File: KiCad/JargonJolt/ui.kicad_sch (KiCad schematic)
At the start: 0 parts

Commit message: worked on pinout
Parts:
- added C1, C2, C3: 0.1uF, symbol Device:C
- added R1, R3, R5: 1k, symbol Device:R
- added R2, R4, R6: 10k, symbol Device:R
- added SW1, SW2, SW3: SW_Push, symbol Switch:SW_Push
- added U1, U2, U3: 40106, symbol 4xxx:40106
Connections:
- new net: R3.2, R4.2, SW2.2
- new net: C1.1, R1.1, U1.1
- new net: R5.2, R6.2, SW3.2
- new net: C3.1, R5.1, U3.1
- new net: R1.2, R2.2, SW1.2
- new net: C2.1, R3.1, U2.1
- new net +3.3V: R2.1, R4.1, R6.1
- new net BUTTON1: U1.2
- new net BUTTON2: U2.2
- new net BUTTON3: U3.2
- new net GND: C1.2, C2.2, C3.2, SW1.1, SW2.1, SW3.1

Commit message: worked on schematic
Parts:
- added J4, J5: Conn_01x08, symbol Connector_Generic:Conn_01x08
- R2, R4, R6: value 10k -> 1M
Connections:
- net GND: now also R2.2, R4.2, R6.2, J4.2 (Pin_2), J5.2 (Pin_2); no longer SW1.1, SW2.1, SW3.1
- removed net +3.3V: R2.1, R4.1, R6.1
- new net: R3.2, R4.1, SW2.1
- new net: R5.2, R6.1, SW3.1
- new net: R1.2, R2.1, SW1.1
- new net +3.3VA: J4.1 (Pin_1), J5.1 (Pin_1), SW2.2, SW3.2
- new net BUSY1: J4.8 (Pin_8)
- new net BUSY2: J5.8 (Pin_8)
- new net CS1: J4.5 (Pin_5)
- new net CS2: J5.5 (Pin_5)
- new net DC1: J4.6 (Pin_6)
- new net DC2: J5.6 (Pin_6)
- new net MOSI: J4.3 (Pin_3), J5.3 (Pin_3)
- new net RST: J4.7 (Pin_7), J5.7 (Pin_7)
- new net SCLK: J4.4 (Pin_4), J5.4 (Pin_4)
- now unconnected: SW1.2
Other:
- note added: "Screen 1 Conn"
- note added: "Screen 2 Conn"
- moved on the sheet: R2, R4, R6, SW1, SW2, SW3

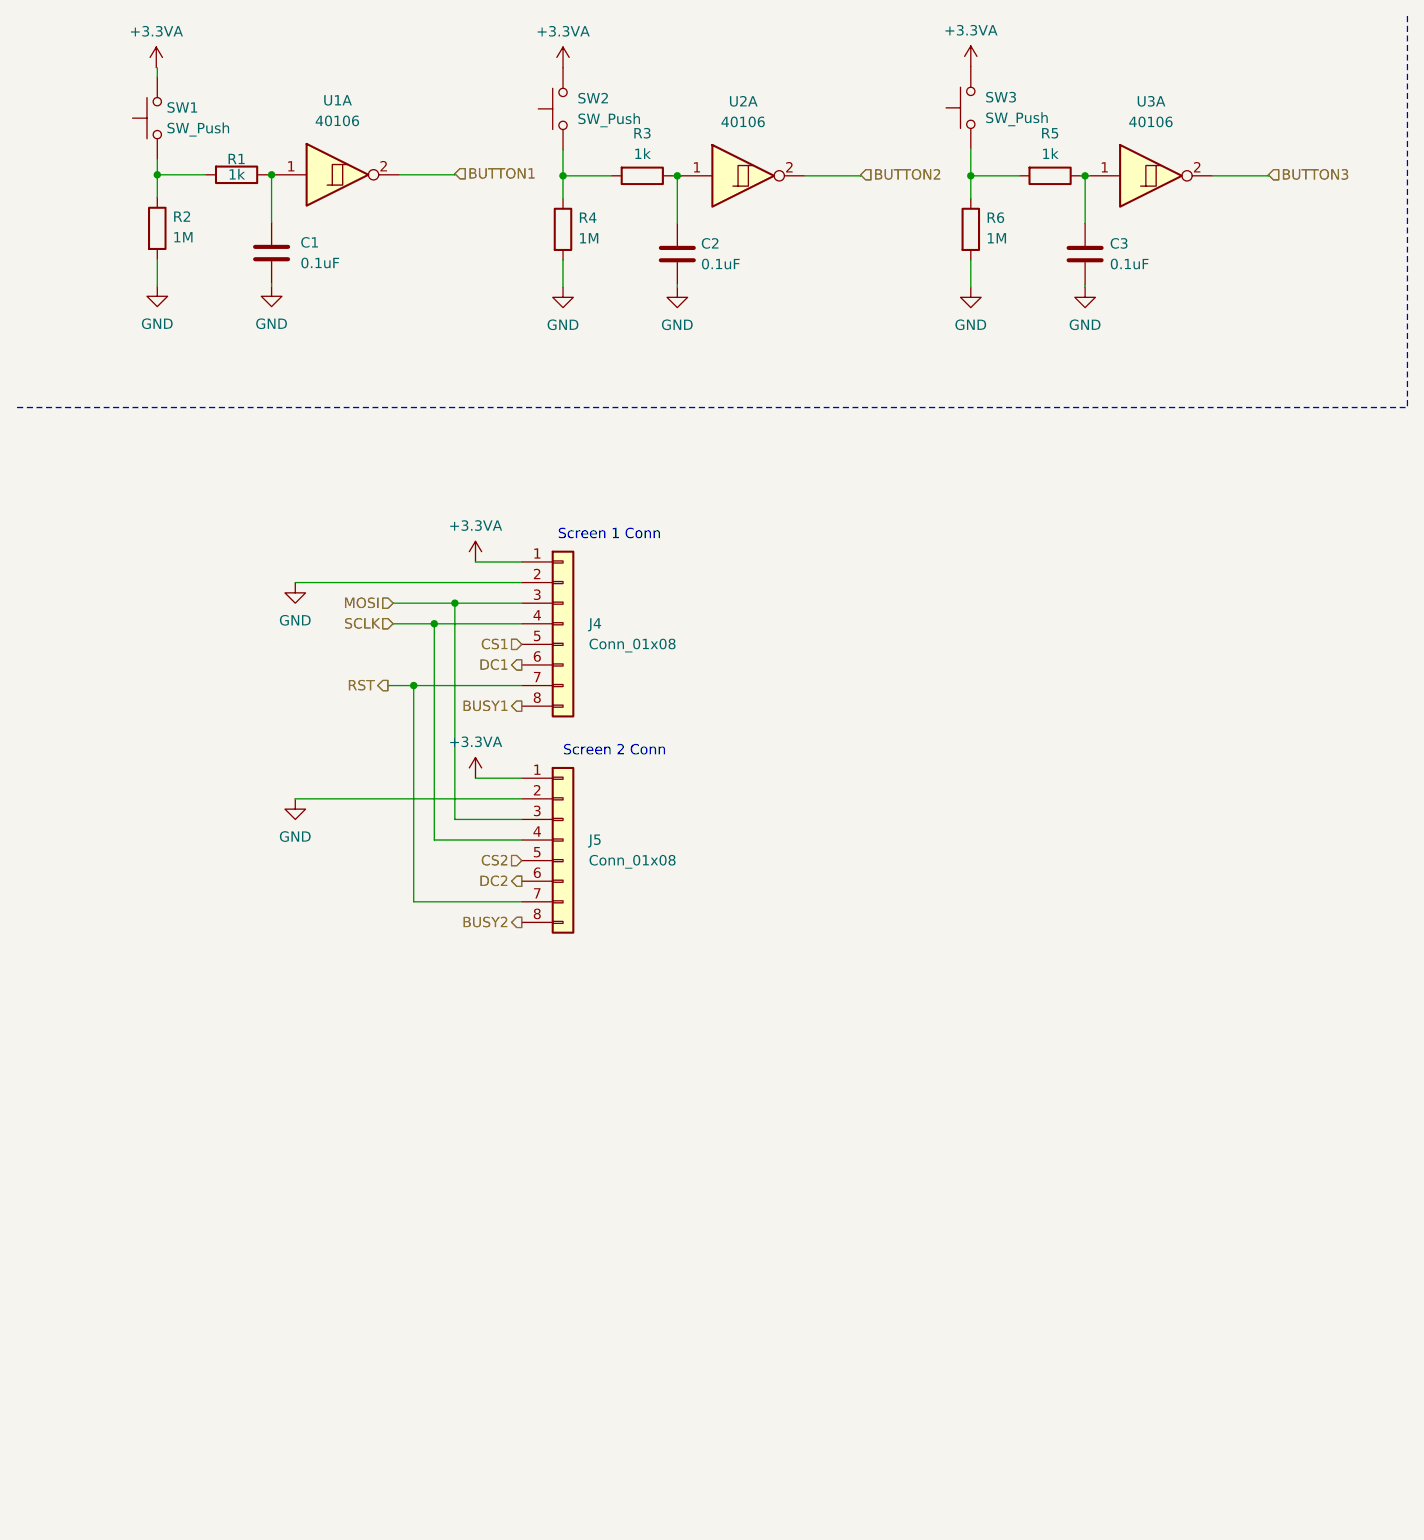
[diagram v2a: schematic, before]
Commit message: added i2s schematic
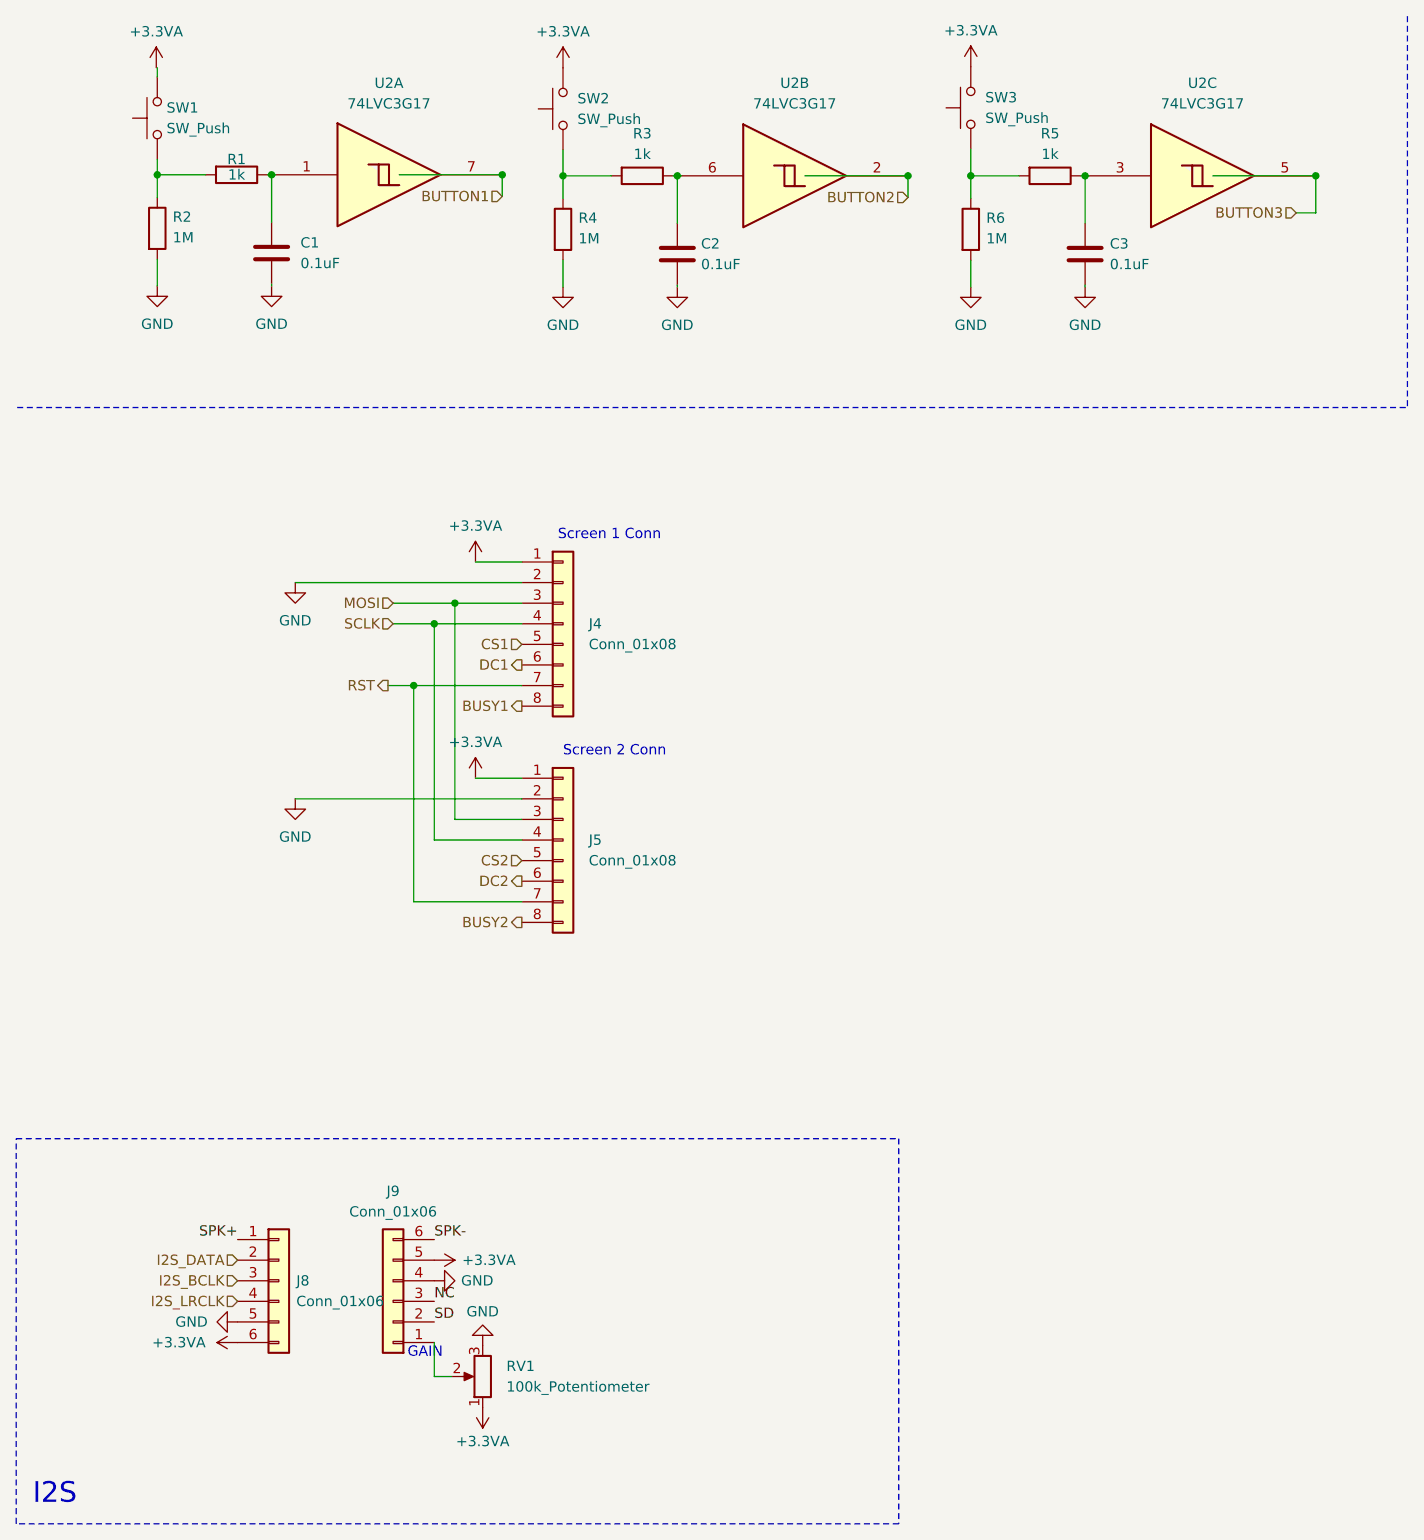
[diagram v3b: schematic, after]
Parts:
- removed U1, U2, U3: 40106, symbol 4xxx:40106
- added J8, J9: Conn_01x06, symbol Connector_Generic:Conn_01x06
- added RV1: 100k_Potentiometer, symbol Device:R_Potentiometer
- added U2: 74LVC3G17, symbol 74xGxx:74LVC3G17
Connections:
- net +3.3VA: now also J8.6 (Pin_6), J9.5 (Pin_5), RV1.1
- net BUTTON1: now also U2.7
- net BUTTON2: now also U2.2
- net BUTTON3: now also U2.5
- net GND: now also J8.5 (Pin_5), J9.4 (Pin_4), RV1.3
- net at C1.1, R1.1: now also U2.1
- net at C3.1, R5.1: now also U2.3
- net at C2.1, R3.1: now also U2.6
- new net: J9.1 (Pin_1), RV1.2
- new net I2S_BCLK: J8.3 (Pin_3)
- new net I2S_DATA: J8.2 (Pin_2)
- new net I2S_LRCLK: J8.4 (Pin_4)
- new net NC: J9.3 (Pin_3)
- new net SD: J9.2 (Pin_2)
- new net SPK+: J8.1 (Pin_1)
- new net SPK-: J9.6 (Pin_6)
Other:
- note added: "GAIN"
- note added: "I2S"

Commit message: added sd module + fixed CS pins
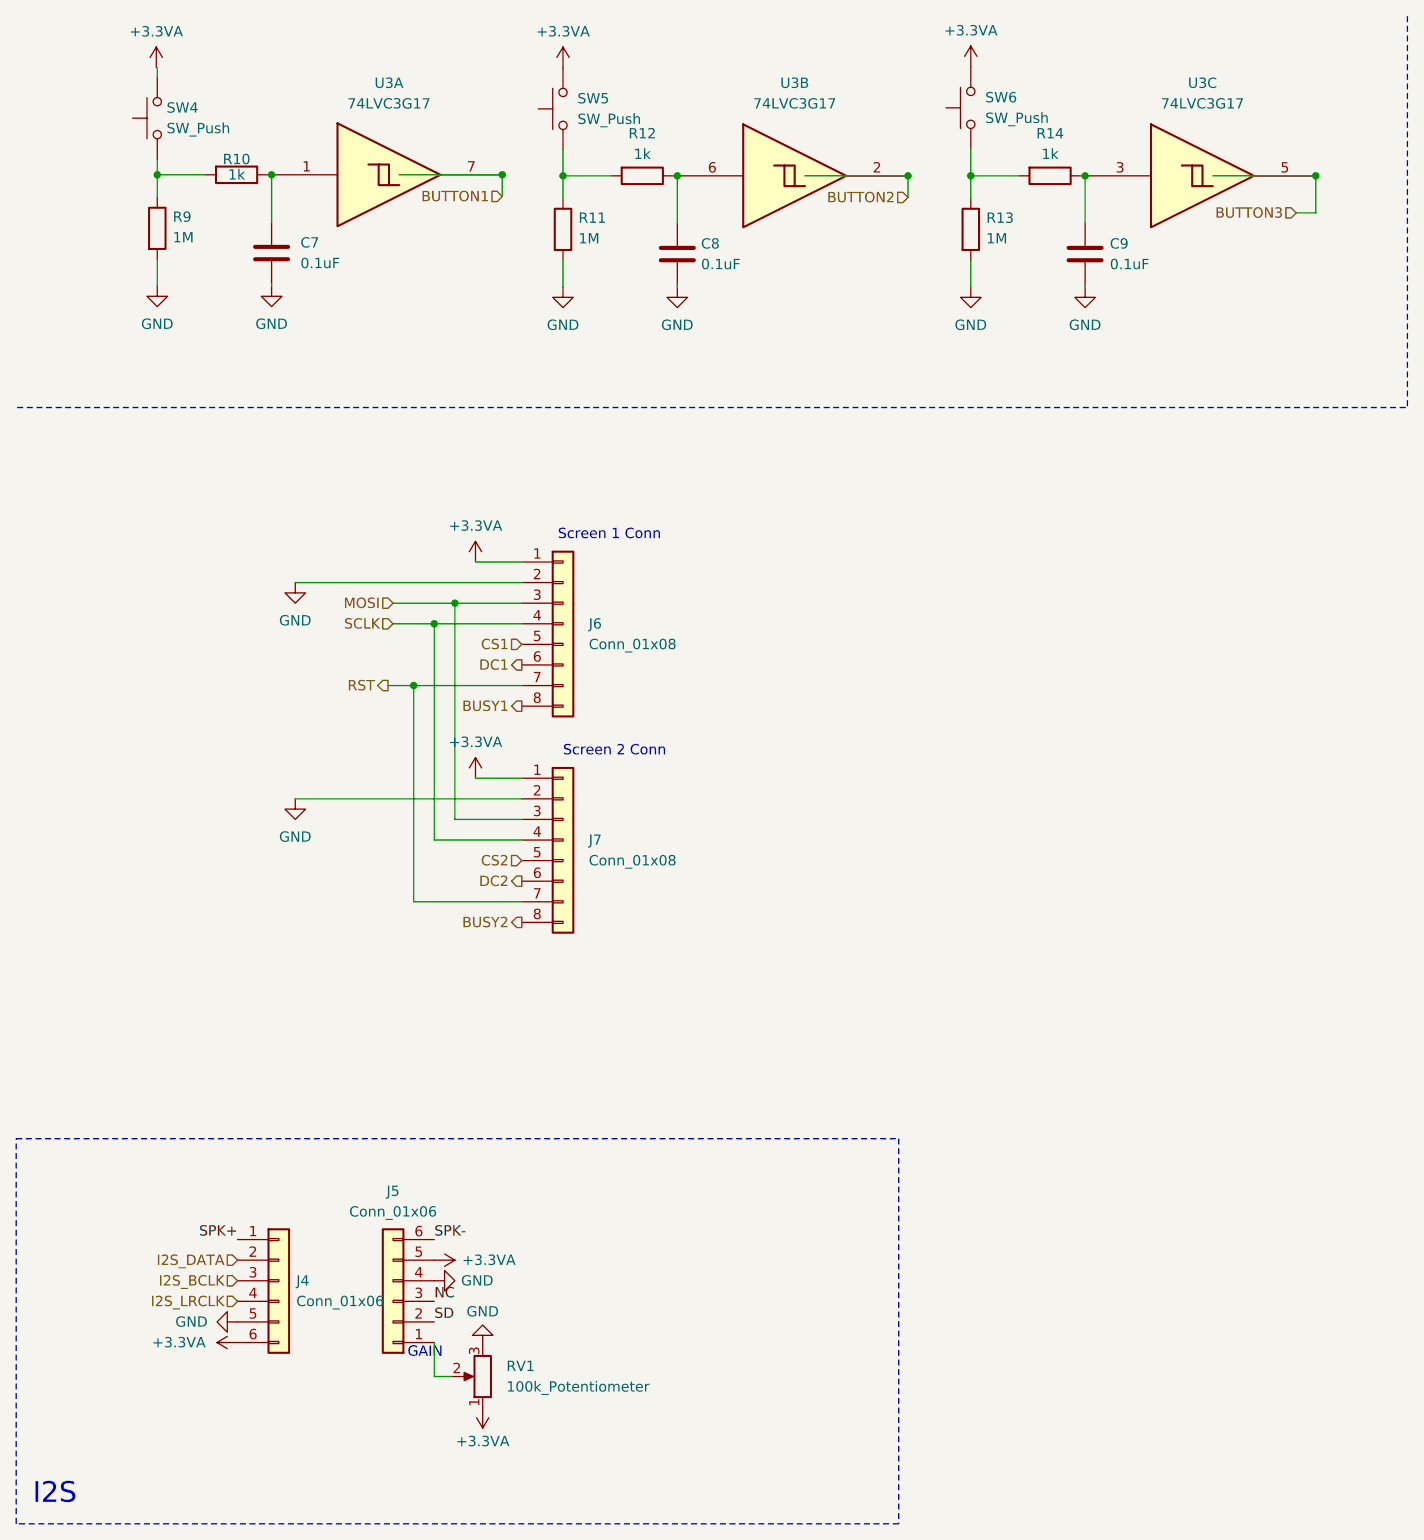
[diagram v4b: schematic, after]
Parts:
- renumbered C1 to C7, C2 to C8, C3 to C9, J8 to J4, J9 to J5, J4 to J6, J5 to J7, R1 to R10, R4 to R11, R3 to R12, R6 to R13, R5 to R14, R2 to R9, SW1 to SW4, SW2 to SW5, SW3 to SW6, U2 to U3

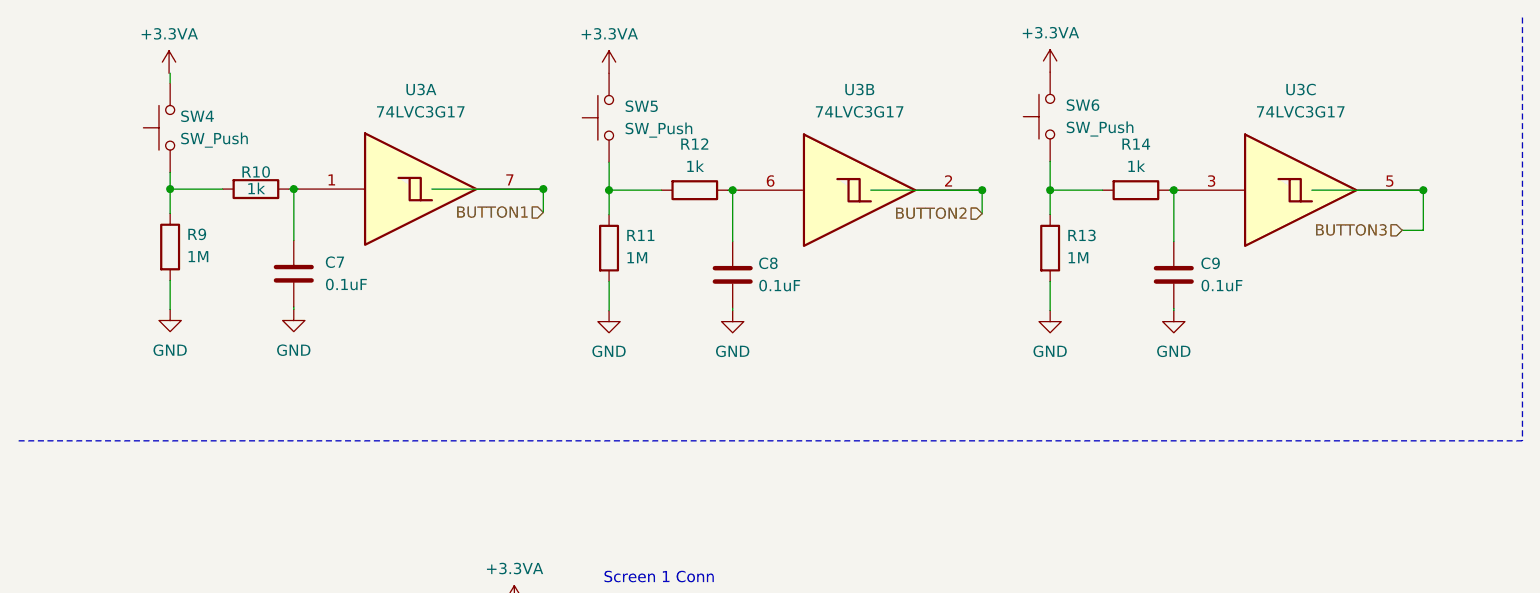
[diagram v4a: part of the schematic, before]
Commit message: added more footprints
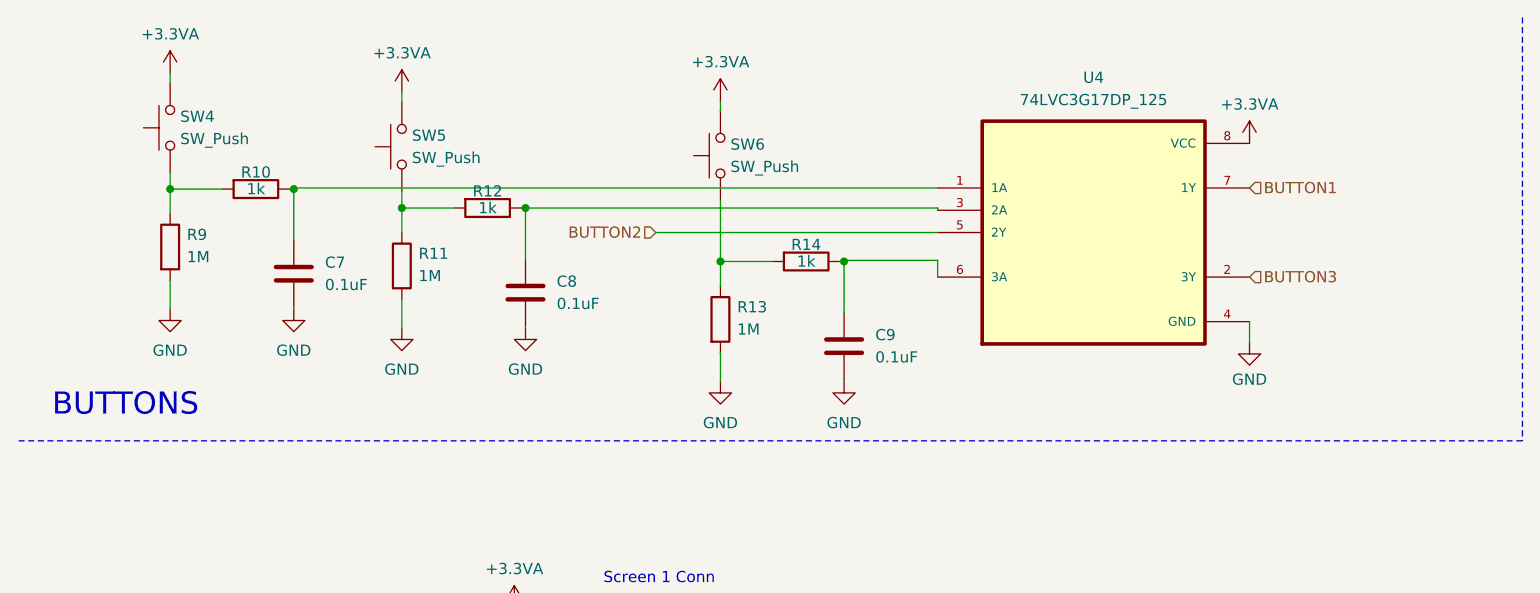
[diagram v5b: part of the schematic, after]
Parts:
- removed U3: 74LVC3G17, symbol 74xGxx:74LVC3G17
- added U4: 74LVC3G17DP_125, Espressif:SOP65P490X110-8N, symbol 74LVC3G17DP_125:74LVC3G17DP_125
- C7, C8, C9: footprint (none) -> Capacitor_SMD:C_0805_2012Metric
- J4, J5: footprint (none) -> Connector_PinHeader_2.54mm:PinHeader_1x06_P2.54mm_Vertical
- J6, J7: footprint (none) -> Connector_PinHeader_2.54mm:PinHeader_1x08_P2.54mm_Vertical
- R10, R11, R12, R13, R14, R9: footprint (none) -> Resistor_SMD:R_0805_2012Metric
- RV1: footprint (none) -> Espressif:TRIM_3296W-1-104LF
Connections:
- net +3.3VA: now also SW4.2, U4.8 (VCC)
- net BUTTON1: now also U4.7 (1Y)
- net BUTTON2: now also U4.5 (2Y)
- net BUTTON3: now also U4.2 (3Y)
- net GND: now also U4.4 (GND)
- net at C7.1, R10.1: now also U4.1 (1A)
- net at C8.1, R12.1: now also U4.3 (2A)
- net at C9.1, R14.1: now also U4.6 (3A)
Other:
- note added: "BUTTONS"
